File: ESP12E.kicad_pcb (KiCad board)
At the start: 2 copper layers, 100 x 100 mm, 129 parts, among them J10 Sol_1, J3 UART, J4 12v PWR, J5 Battery, J6 Sol_2, J7 Sol_3, J8 Sol_4, J9 Motor, Q1 RU3560L, Q2 IRF540N, Q3 IRF540N, Q4 IRF540N, Q5 IRF540N, Q6 IRF540N, Q7 2SJ174, Q8 2SJ174, Q9 2SJ174, U1 MPS-2108, U10 TLP250, U11 TLP250, U12 TLP250, U13 LTC2952, U14 AMS1117-3.3, U15 LM7805_TO220, U16 CN3703, U2 HX710(A/B), U3 MPS-2108, U4 HX710(A/B), U5 AMS1117-3.3, U6 LM7805_TO220, U7 ESP-12E, U8 TLP250, U9 TLP250

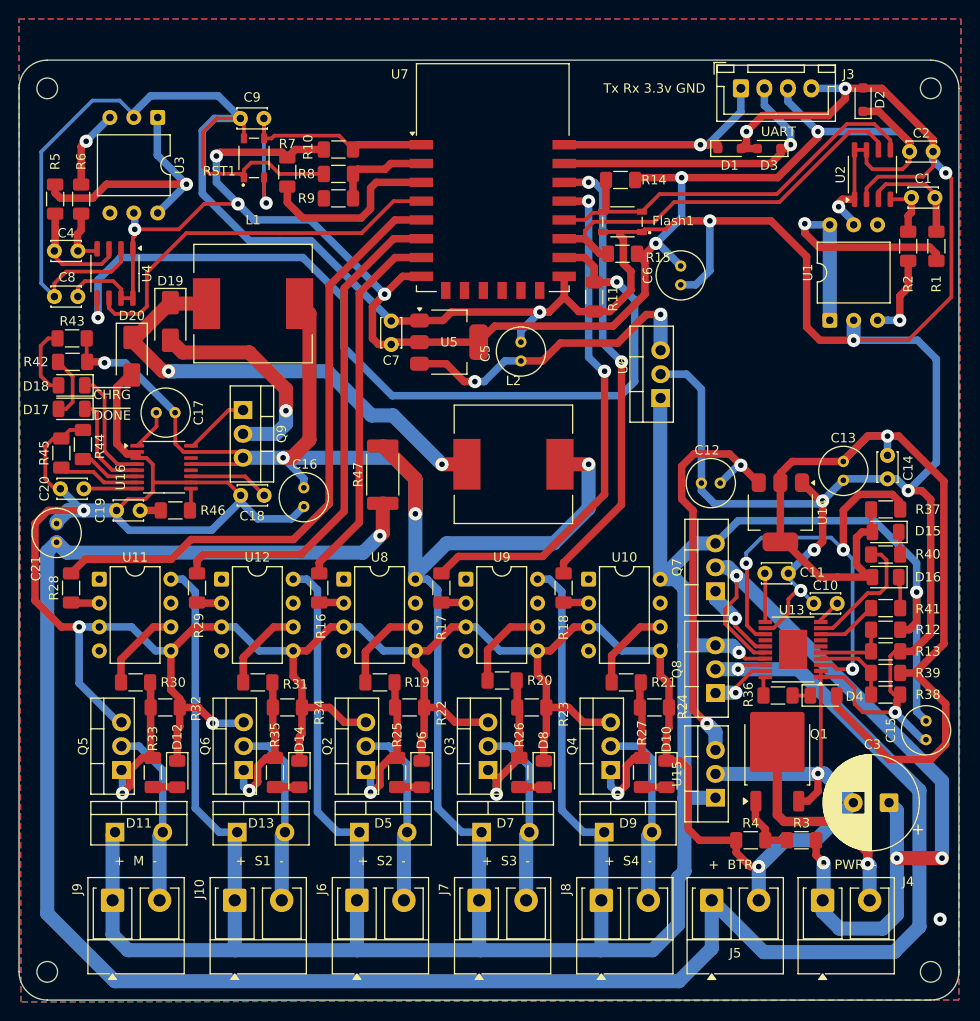
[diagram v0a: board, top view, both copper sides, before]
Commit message: Final: small edit on silkscreen + BOM file + generating Gerber file.
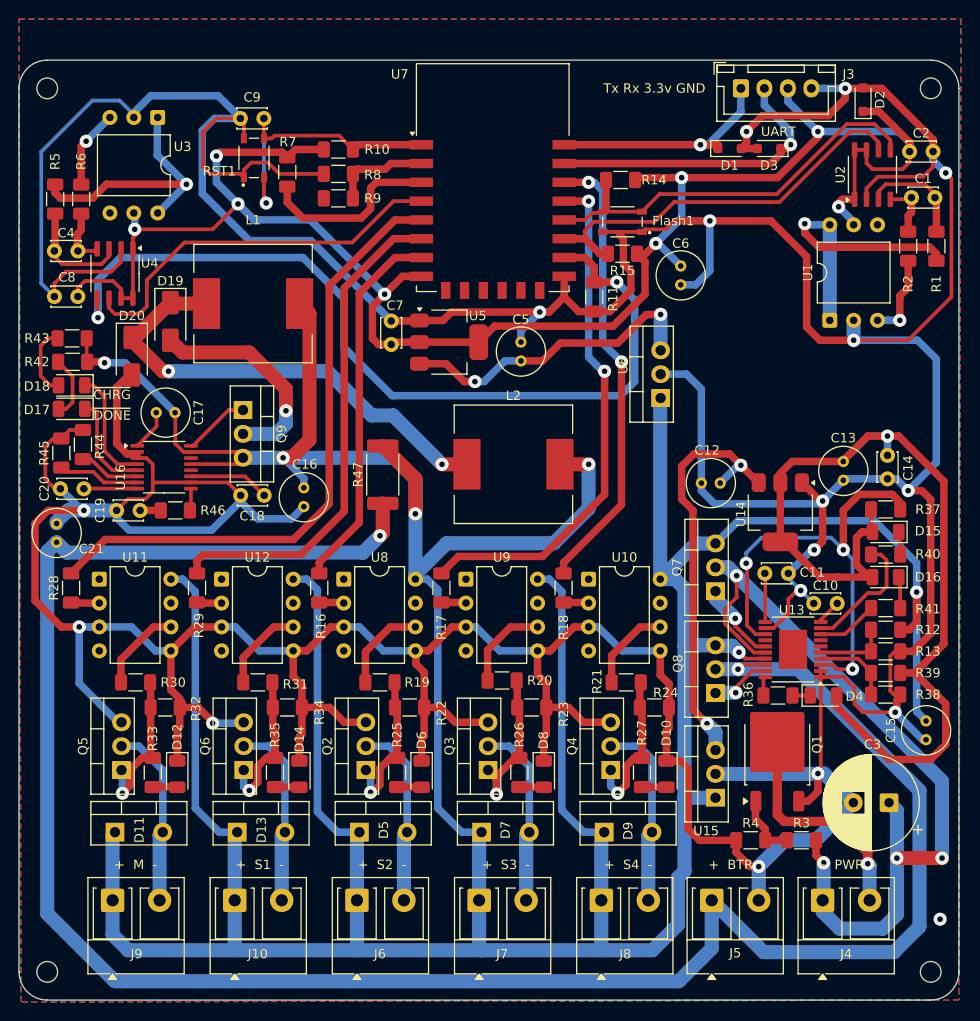
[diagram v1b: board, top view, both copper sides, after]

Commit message: fix: more Via for better soldering on local production PCB.
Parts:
- moved R46 1.57 mm to (43.2, 67.9)
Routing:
- net GND: track 754.0 -> 794.1 mm, vias 17 -> 27
- net PWR_{out}: track 499.5 -> 483.4 mm, vias 6 -> 7
- net Net-(R31-Pad1): track 9.31 -> 24.1 mm, vias 0 -> 1
- net Net-(R30-Pad1): track 9.19 -> 23.8 mm, vias 0 -> 1
- net Net-(R21-Pad1): track 9.28 -> 23.8 mm, vias 0 -> 1
- net Net-(R20-Pad1): track 9.58 -> 23.8 mm, vias 0 -> 1
- net Net-(R19-Pad1): track 9.66 -> 23.8 mm, vias 0 -> 1
- net +3.3V: track 193.3 -> 205.4 mm, vias 8 -> 10
- net Net-(U9-A): track 2.63 -> 12.3 mm, vias 0 -> 1
- net Net-(U8-A): track 2.63 -> 11.9 mm, vias 0 -> 1
- net Net-(U12-A): track 2.63 -> 11.8 mm, vias 0 -> 1
- net Net-(U10-A): track 2.68 -> 11.5 mm, vias 0 -> 1
- net Net-(Q3-G): track 16.4 -> 22.7 mm
- net Net-(Q6-G): track 16.2 -> 22.4 mm
- net Net-(Q4-G): track 16.3 -> 22.2 mm
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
